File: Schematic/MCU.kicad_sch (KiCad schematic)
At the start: 21 parts, among them IC3 STM32H743VIT6, SW1 TS24CA, Y1 8MHz

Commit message: minor update and some checking
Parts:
- C1, C53: MPN (none) -> 02016D225MAT2A; Manufacturer (none) -> KYOCERA AVX
- C2, C5, C6, C7, C8, C9: MPN (none) -> C0603X5R1E104K030BB; Manufacturer (none) -> TDK
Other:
- note added: "USB-C connector for configuring firmware and 5V supply"
- moved on the sheet: C1, R6, R7, USB1

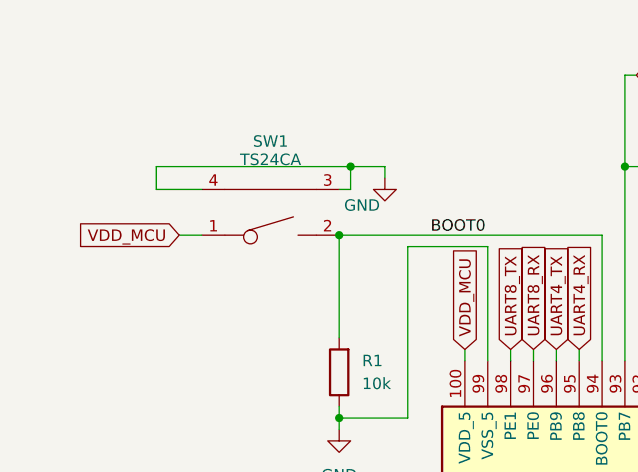
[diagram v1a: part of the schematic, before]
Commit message: remove switch to use jumper for bootloader activation
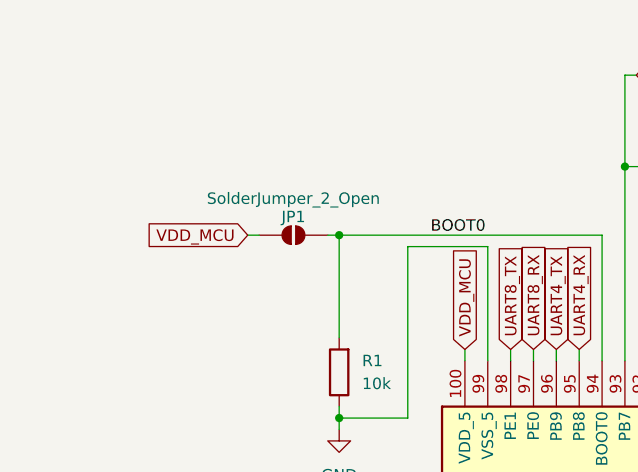
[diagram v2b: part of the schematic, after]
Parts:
- removed SW1: TS24CA, fch7:SW-SMD_2P-TS24CA, symbol fclib:TS24CA
- added JP1: SolderJumper_2_Open, Jumper:SolderJumper-2_P1.3mm_Open_RoundedPad1.0x1.5mm, symbol Jumper:SolderJumper_2_Open
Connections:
- net BOOT0: now also JP1.2 (B)
- net VDD_MCU: now also JP1.1 (A)

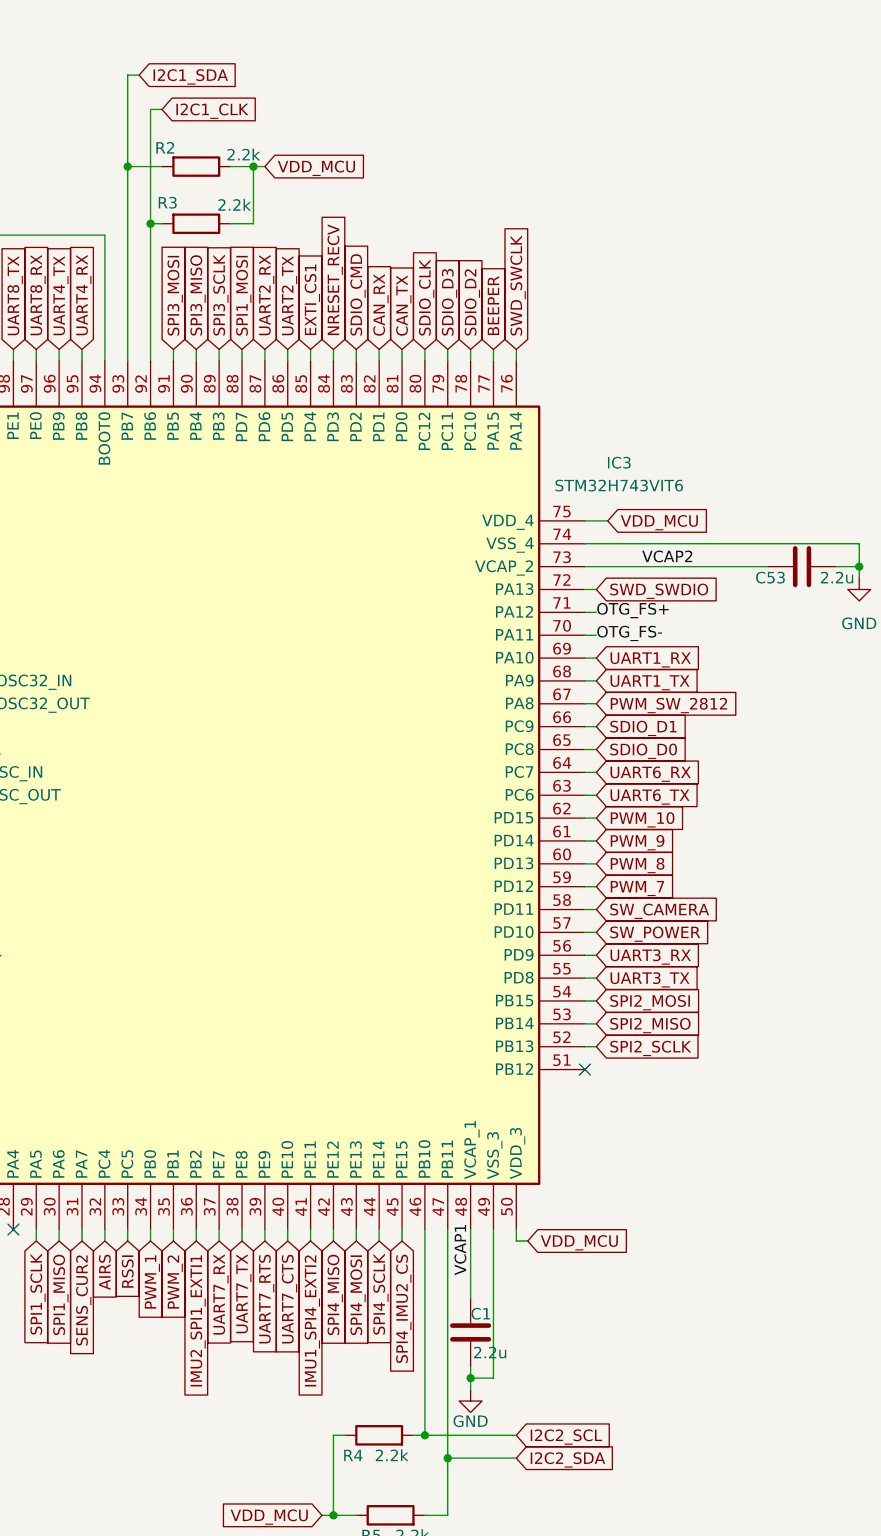
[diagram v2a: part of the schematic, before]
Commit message: optimisation : - refactoring two 4 pin connector for mag and gps into one 6 pin connector - increased output voltage from 5V buck regulator to take into account voltage decrease schottky diodes
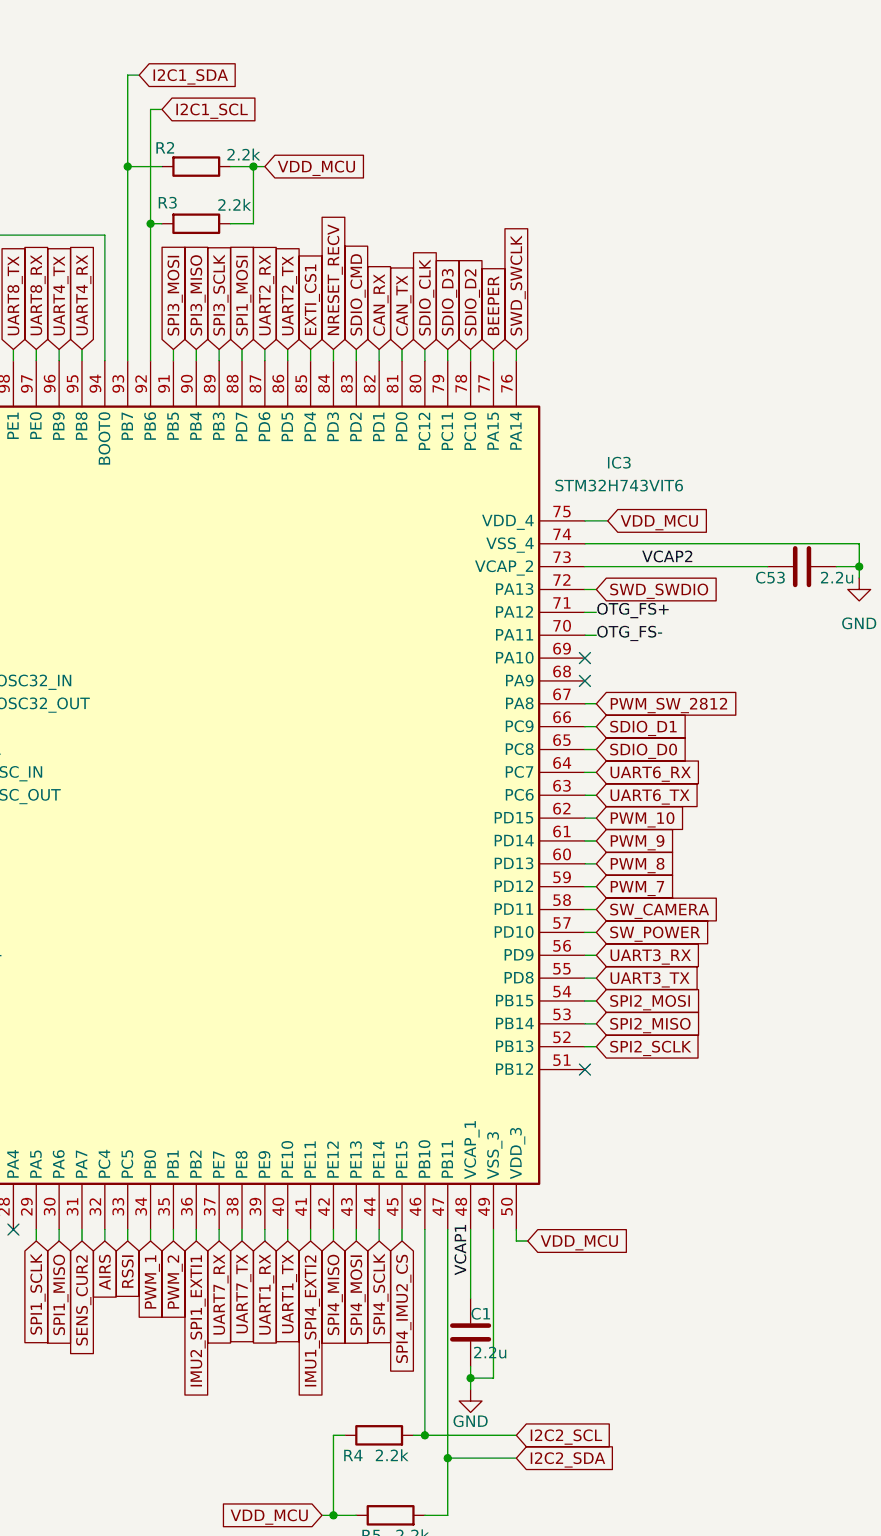
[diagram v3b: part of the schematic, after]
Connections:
- net UART7_CTS is gone; now on net UART1_TX: IC3.40 (PE10)
- net UART7_RTS is gone; now on net UART1_RX: IC3.39 (PE9)
- net UART1_RX: no longer IC3.69 (PA10)
- net UART1_TX: no longer IC3.68 (PA9)
- net I2C1_CLK renamed I2C1_SCL
- no-connect marks 8 -> 10

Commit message: update on routing
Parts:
- C1, C10, C11, C2, C5, C53, C6, C7, C8, C9: footprint Capacitor_SMD:C_0603_1608Metric -> Capacitor_SMD:C_0402_1005Metric
- R1, R2, R3, R4, R5, R6, R7: footprint Resistor_SMD:R_0603_1608Metric -> Resistor_SMD:R_0402_1005Metric
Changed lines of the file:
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@@
 			)
 		)
-		(property "Footprint" "Capacitor_SMD:C_0603_1608Metric"
+		(property "Footprint" "Capacitor_SMD:C_0402_1005Metric"
 			(at 267.6652 38.1 0)
 			(effects
@@
 			)
 		)
-		(property "Footprint" "Capacitor_SMD:C_0603_1608Metric"
+		(property "Footprint" "Capacitor_SMD:C_0402_1005Metric"
 			(at 46.6852 111.76 0)
 			(effects
@@
 			)
 		)
-		(property "Footprint" "Resistor_SMD:R_0603_1608Metric"
+		(property "Footprint" "Resistor_SMD:R_0402_1005Metric"
 			(at 58.928 52.07 90)
 			(effects
@@
 			)
 		)
-		(property "Footprint" "Capacitor_SMD:C_0603_1608Metric"
+		(property "Footprint" "Capacitor_SMD:C_0402_1005Metric"
 			(at 256.2352 38.1 0)
 			(effects
@@
 			)
 		)
-		(property "Footprint" "Capacitor_SMD:C_0603_1608Metric"
+		(property "Footprint" "Capacitor_SMD:C_0402_1005Metric"
 			(at 221.9452 38.1 0)
 			(effects
@@
 			)
 		)
-		(property "Footprint" "Capacitor_SMD:C_0603_1608Metric"
+		(property "Footprint" "Capacitor_SMD:C_0402_1005Metric"
 			(at 167.64 72.6948 0)
 			(effects
@@
 			)
 		)
-		(property "Footprint" "Capacitor_SMD:C_0603_1608Metric"
+		(property "Footprint" "Capacitor_SMD:C_0402_1005Metric"
 			(at 233.3752 38.1 0)
 			(effects
@@
 			)
 		)
-		(property "Footprint" "Resistor_SMD:R_0603_1608Metric"
+		(property "Footprint" "Resistor_SMD:R_0402_1005Metric"
 			(at 96.52 27.432 90)
 			(effects
@@
 			)
 		)
-		(property "Footprint" "Resistor_SMD:R_0603_1608Metric"
+		(property "Footprint" "Resistor_SMD:R_0402_1005Metric"
 			(at 118.11 180.848 90)
 			(effects
@@
 			)
 		)
-		(property "Footprint" "Capacitor_SMD:C_0603_1608Metric"
+		(property "Footprint" "Capacitor_SMD:C_0402_1005Metric"
 			(at 244.8052 38.1 0)
 			(effects
@@
 			)
 		)
-		(property "Footprint" "Resistor_SMD:R_0603_1608Metric"
+		(property "Footprint" "Resistor_SMD:R_0402_1005Metric"
 			(at 96.52 33.782 90)
 			(effects
@@
 			)
 		)
-		(property "Footprint" "Resistor_SMD:R_0603_1608Metric"
+		(property "Footprint" "Resistor_SMD:R_0402_1005Metric"
 			(at 116.84 171.958 90)
 			(effects
@@
 			)
 		)
-		(property "Footprint" "Resistor_SMD:R_0603_1608Metric"
+		(property "Footprint" "Resistor_SMD:R_0402_1005Metric"
 			(at 218.44 92.202 90)
 			(effects
@@
 			)
 		)
-		(property "Footprint" "Resistor_SMD:R_0603_1608Metric"
+		(property "Footprint" "Resistor_SMD:R_0402_1005Metric"
 			(at 220.98 107.442 90)
 			(effects
@@
 			)
 		)
-		(property "Footprint" "Capacitor_SMD:C_0603_1608Metric"
+		(property "Footprint" "Capacitor_SMD:C_0402_1005Metric"
 			(at 199.0852 38.1 0)
 			(effects
@@
 			)
 		)
-		(property "Footprint" "Capacitor_SMD:C_0603_1608Metric"
+		(property "Footprint" "Capacitor_SMD:C_0402_1005Metric"
 			(at 210.5152 38.1 0)
 			(effects
@@
 			)
 		)
-		(property "Footprint" "Capacitor_SMD:C_0603_1608Metric"
+		(property "Footprint" "Capacitor_SMD:C_0402_1005Metric"
 			(at 127.9652 162.56 0)
 			(effects
